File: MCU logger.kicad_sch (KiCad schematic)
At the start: 25 parts, among them U1 24LC1025, U2 24LC1025, U3 DS1337S_, U4 ATMEGA328P-AU, Y1 Crystal, Y2 Crystal

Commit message: value of components
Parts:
- C1, C2: value C -> 0.1 uF
- C3, C4: value C -> 22 pF
- C5: value C_Polarized -> 100 nF
- R1, R2: value R -> 330
- R3, R4: value R -> 10 K
- R5, R6: value R -> 4.7 K
- R7: value R -> 10 k
- Y1: value Crystal -> 16 MHz
- Y2: value Crystal -> 32.768 KHz
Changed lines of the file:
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@@
 			)
 		)
-		(property "Value" "R"
+		(property "Value" "4.7 K"
 			(at 120.65 173.9899 0)
 			(show_name no)
@@
 		)
 		(property "Description" "Resistor"
+			(at 118.11 172.72 0)
+			(hide yes)
+			(show_name no)
+			(do_not_autoplace no)
+			(effects
+				(font
+					(size 1.27 1.27)
+				)
+			)
+		)
+		(property "purpose" ""
 			(at 118.11 172.72 0)
 			(hide yes)
@@
 			)
 		)
-		(property "Value" "R"
+		(property "Value" "330"
 			(at 246.38 71.1199 0)
 			(show_name no)
@@
 		)
 		(property "Description" "Resistor"
+			(at 243.84 69.85 0)
+			(hide yes)
+			(show_name no)
+			(do_not_autoplace no)
+			(effects
+				(font
+					(size 1.27 1.27)
+				)
+			)
+		)
+		(property "purpose" ""
 			(at 243.84 69.85 0)
 			(hide yes)
@@
 			)
 		)
+		(property "purpose" ""
+			(at 262.89 38.1 0)
+			(hide yes)
+			(show_name no)
+			(do_not_autoplace no)
+			(effects
+				(font
+					(size 1.27 1.27)
+				)
+			)
+		)
 		(pin "2"
 		)
@@
 			)
 		)
-		(property "Value" "C"
+		(property "Value" "22 pF"
 			(at 176.53 69.8499 0)
 			(show_name no)
@@
 		)
 		(property "Description" "Unpolarized capacitor"
+			(at 172.72 68.58 0)
+			(hide yes)
+			(show_name no)
+			(do_not_autoplace no)
+			(effects
+				(font
+					(size 1.27 1.27)
+				)
+			)
+		)
+		(property "purpose" ""
 			(at 172.72 68.58 0)
 			(hide yes)
@@
 			)
 		)
-		(property "Value" "R"
+		(property "Value" "10 K"
 			(at 106.68 52.0699 0)
 			(show_name no)
@@
 		)
 		(property "Description" "Resistor"
+			(at 104.14 50.8 0)
+			(hide yes)
+			(show_name no)
+			(do_not_autoplace no)
+			(effects
+				(font
+					(size 1.27 1.27)
+				)
+			)
+		)
+		(property "purpose" ""
 			(at 104.14 50.8 0)
 			(hide yes)
@@
 			)
 		)
-		(property "Value" "R"
+		(property "Value" "330"
 			(at 171.45 39.37 90)
 			(show_name no)
@@
 		)
 		(property "Description" "Resistor"
+			(at 171.45 43.18 0)
+			(hide yes)
+			(show_name no)
+			(do_not_autoplace no)
+			(effects
+				(font
+					(size 1.27 1.27)
+				)
+			)
+		)
+		(property "purpose" ""
 			(at 171.45 43.18 0)
 			(hide yes)
@@
 			)
 		)
-		(property "Value" "R"
+		(property "Value" "4.7 K"
 			(at 109.22 173.9899 0)
 			(show_name no)
@@
 		)
 		(property "Description" "Resistor"
+			(at 106.68 172.72 0)
+			(hide yes)
+			(show_name no)
+			(do_not_autoplace no)
+			(effects
+				(font
+					(size 1.27 1.27)
+				)
+			)
+		)
+		(property "purpose" ""
 			(at 106.68 172.72 0)
 			(hide yes)
@@
 			)
 		)
-		(property "Value" "C_Polarized"
+		(property "Value" "100 nF"
 			(at 247.65 38.4809 0)
 			(show_name no)
@@
 		)
 		(property "Description" "Polarized capacitor"
+			(at 243.84 38.1 0)
+			(hide yes)
+			(show_name no)
+			(do_not_autoplace no)
+			(effects
+				(font
+					(size 1.27 1.27)
+				)
+			)
+		)
+		(property "purpose" ""
 			(at 243.84 38.1 0)
 			(hide yes)
@@
 			)
 		)
-		(property "Value" "Crystal"
+		(property "Value" "32.768 KHz"
 			(at 43.18 50.8 0)
 			(show_name no)
@@
 		)
 		(property "Description" "Two pin crystal"
+			(at 43.18 55.88 0)
+			(hide yes)
+			(show_name no)
+			(do_not_autoplace no)
+			(effects
+				(font
+					(size 1.27 1.27)
+				)
+			)
+		)
+		(property "purpose" ""
 			(at 43.18 55.88 0)
 			(hide yes)
@@
 			)
 		)
-		(property "Value" "C"
+		(property "Value" "0.1 uF"
 			(at 187.96 31.7499 0)
 			(show_name no)
@@
 		)
 		(property "Description" "Unpolarized capacitor"
+			(at 184.15 30.48 0)
+			(hide yes)
+			(show_name no)
+			(do_not_autoplace no)
+			(effects
+				(font
+					(size 1.27 1.27)
+				)
+			)
+		)
+		(property "purpose" ""
 			(at 184.15 30.48 0)
 			(hide yes)
@@
 			)
 		)
-		(property "Value" "R"
+		(property "Value" "10 K"
 			(at 118.11 52.0699 0)
 			(show_name no)
@@
 		)
 		(property "Description" "Resistor"
+			(at 115.57 50.8 0)
+			(hide yes)
+			(show_name no)
+			(do_not_autoplace no)
+			(effects
+				(font
+					(size 1.27 1.27)
+				)
+			)
+		)
+		(property "purpose" ""
 			(at 115.57 50.8 0)
 			(hide yes)
@@
 			)
 		)
-		(property "Value" "R"
+		(property "Value" "10 k"
 			(at 189.23 74.93 90)
 			(show_name no)
@@
 		)
 		(property "Description" "Resistor"
+			(at 189.23 78.74 0)
+			(hide yes)
+			(show_name no)
+			(do_not_autoplace no)
+			(effects
+				(font
+					(size 1.27 1.27)
+				)
+			)
+		)
+		(property "purpose" ""
 			(at 189.23 78.74 0)
 			(hide yes)
@@
 			)
 		)
-		(property "Value" "C"
+		(property "Value" "0.1 uF"
 			(at 128.27 52.0699 0)
 			(show_name no)
@@
 		)
 		(property "Description" "Unpolarized capacitor"
+			(at 124.46 50.8 0)
+			(hide yes)
+			(show_name no)
+			(do_not_autoplace no)
+			(effects
+				(font
+					(size 1.27 1.27)
+				)
+			)
+		)
+		(property "purpose" ""
 			(at 124.46 50.8 0)
 			(hide yes)
@@
 			)
 		)
-		(property "Value" "C"
+		(property "Value" "22 pF"
 			(at 176.53 55.8799 0)
 			(show_name no)
@@
 		)
 		(property "Description" "Unpolarized capacitor"
+			(at 172.72 54.61 0)
+			(hide yes)
+			(show_name no)
+			(do_not_autoplace no)
+			(effects
+				(font
+					(size 1.27 1.27)
+				)
+			)
+		)
+		(property "purpose" ""
 			(at 172.72 54.61 0)
 			(hide yes)
@@
 			)
 		)
-		(property "Value" "Crystal"
+		(property "Value" "16 MHz"
 			(at 184.15 55.88 0)
 			(show_name no)
@@
 			(at 184.15 60.96 0)
 			(hide yes)
+			(show_name no)
+			(do_not_autoplace no)
+			(effects
+				(font
+					(size 1.27 1.27)
+				)
+			)
+		)
+		(property "purpose" ""
+			(at 184.15 60.96 0)
+			(hide yes)

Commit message: footprint assigned
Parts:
- BT1: footprint (none) -> Connector_PinHeader_2.54mm:PinHeader_1x02_P2.54mm_Vertical
- C1, C2, C3, C4, C5: footprint (none) -> Capacitor_SMD:C_0805_2012Metric
- D1, D2: footprint (none) -> LED_SMD:LED_0805_2012Metric
- H1, H2, H3, H4: footprint (none) -> MountingHole:MountingHole_2.1mm
- R1, R2, R3, R4, R5, R6, R7: footprint (none) -> Resistor_SMD:R_0805_2012Metric
- U1, U2: footprint (none) -> Package_SO:SOIC-8_5.3x5.3mm_P1.27mm
- U3: footprint DS1337S_:SOIC127P600X175-8N -> footprints:SOIC127P600X175-8N
- U4: footprint ATMEGA328P-AU:QFP80P900X900X120-32N -> footprints:QFP80P900X900X120-32N
- Y1, Y2: footprint (none) -> Crystal:Crystal_SMD_5032-2Pin_5.0x3.2mm_HandSoldering
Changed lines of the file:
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@@
 			)
 		)
-		(property "Footprint" ""
+		(property "Footprint" "MountingHole:MountingHole_2.1mm"
 			(at 247.65 154.94 0)
 			(hide yes)
@@
 			)
 		)
-		(property "Footprint" ""
+		(property "Footprint" "Resistor_SMD:R_0805_2012Metric"
 			(at 116.332 172.72 90)
 			(hide yes)
@@
 			)
 		)
-		(property "Footprint" ""
+		(property "Footprint" "LED_SMD:LED_0805_2012Metric"
 			(at 243.84 53.34 0)
 			(hide yes)
@@
 			)
 		)
-		(property "Footprint" ""
+		(property "Footprint" "MountingHole:MountingHole_2.1mm"
 			(at 247.65 124.46 0)
 			(hide yes)
@@
 			)
 		)
-		(property "Footprint" ""
+		(property "Footprint" "Resistor_SMD:R_0805_2012Metric"
 			(at 242.062 69.85 90)
 			(hide yes)
@@
 			)
 		)
-		(property "Footprint" ""
+		(property "Footprint" "Connector_PinHeader_2.54mm:PinHeader_1x02_P2.54mm_Vertical"
 			(at 262.89 36.576 90)
 			(hide yes)
@@
 			)
 		)
-		(property "Footprint" ""
+		(property "Footprint" "Capacitor_SMD:C_0805_2012Metric"
 			(at 173.6852 72.39 0)
 			(hide yes)
@@
 			)
 		)
-		(property "Footprint" ""
+		(property "Footprint" "Resistor_SMD:R_0805_2012Metric"
 			(at 102.362 50.8 90)
 			(hide yes)
@@
 			)
 		)
-		(property "Footprint" "DS1337S_:SOIC127P600X175-8N"
+		(property "Footprint" "footprints:SOIC127P600X175-8N"
 			(at 76.2 60.96 0)
 			(hide yes)
@@
 			)
 		)
-		(property "Footprint" ""
+		(property "Footprint" "Resistor_SMD:R_0805_2012Metric"
 			(at 171.45 44.958 90)
 			(hide yes)
@@
 			)
 		)
-		(property "Footprint" ""
+		(property "Footprint" "Resistor_SMD:R_0805_2012Metric"
 			(at 104.902 172.72 90)
 			(hide yes)
@@
 			)
 		)
-		(property "Footprint" ""
+		(property "Footprint" "Package_SO:SOIC-8_5.3x5.3mm_P1.27mm"
 			(at 87.63 173.99 0)
 			(hide yes)
@@
 			)
 		)
-		(property "Footprint" ""
+		(property "Footprint" "Package_SO:SOIC-8_5.3x5.3mm_P1.27mm"
 			(at 53.34 173.99 0)
 			(hide yes)
@@
 			)
 		)
-		(property "Footprint" ""
+		(property "Footprint" "MountingHole:MountingHole_2.1mm"
 			(at 247.65 134.62 0)
 			(hide yes)
@@
 			)
 		)
-		(property "Footprint" "ATMEGA328P-AU:QFP80P900X900X120-32N"
+		(property "Footprint" "footprints:QFP80P900X900X120-32N"
 			(at 214.63 58.42 0)
 			(hide yes)
@@
 			)
 		)
-		(property "Footprint" ""
+		(property "Footprint" "MountingHole:MountingHole_2.1mm"
 			(at 247.65 144.78 0)
 			(hide yes)
@@
 			)
 		)
-		(property "Footprint" ""
+		(property "Footprint" "Capacitor_SMD:C_0805_2012Metric"
 			(at 244.8052 41.91 0)
 			(hide yes)
@@
 			)
 		)
-		(property "Footprint" ""
+		(property "Footprint" "Crystal:Crystal_SMD_5032-2Pin_5.0x3.2mm_HandSoldering"
 			(at 43.18 55.88 0)
 			(hide yes)
@@
 			)
 		)
-		(property "Footprint" ""
+		(property "Footprint" "Capacitor_SMD:C_0805_2012Metric"
 			(at 185.1152 34.29 0)
 			(hide yes)
@@
 			)
 		)
-		(property "Footprint" ""
+		(property "Footprint" "Resistor_SMD:R_0805_2012Metric"
 			(at 113.792 50.8 90)
 			(hide yes)
@@
 			)
 		)
-		(property "Footprint" ""
+		(property "Footprint" "LED_SMD:LED_0805_2012Metric"
 			(at 184.15 43.18 0)
 			(hide yes)
@@
 			)
 		)
-		(property "Footprint" ""
+		(property "Footprint" "Resistor_SMD:R_0805_2012Metric"
 			(at 189.23 80.518 90)
 			(hide yes)
@@
 			)
 		)
-		(property "Footprint" ""
+		(property "Footprint" "Capacitor_SMD:C_0805_2012Metric"
 			(at 125.4252 54.61 0)
 			(hide yes)
@@
 			)
 		)
-		(property "Footprint" ""
+		(property "Footprint" "Capacitor_SMD:C_0805_2012Metric"
 			(at 173.6852 58.42 0)
 			(hide yes)
@@
 			)
 		)
-		(property "Footprint" ""
+		(property "Footprint" "Crystal:Crystal_SMD_5032-2Pin_5.0x3.2mm_HandSoldering"
 			(at 184.15 60.96 0)
 			(hide yes)

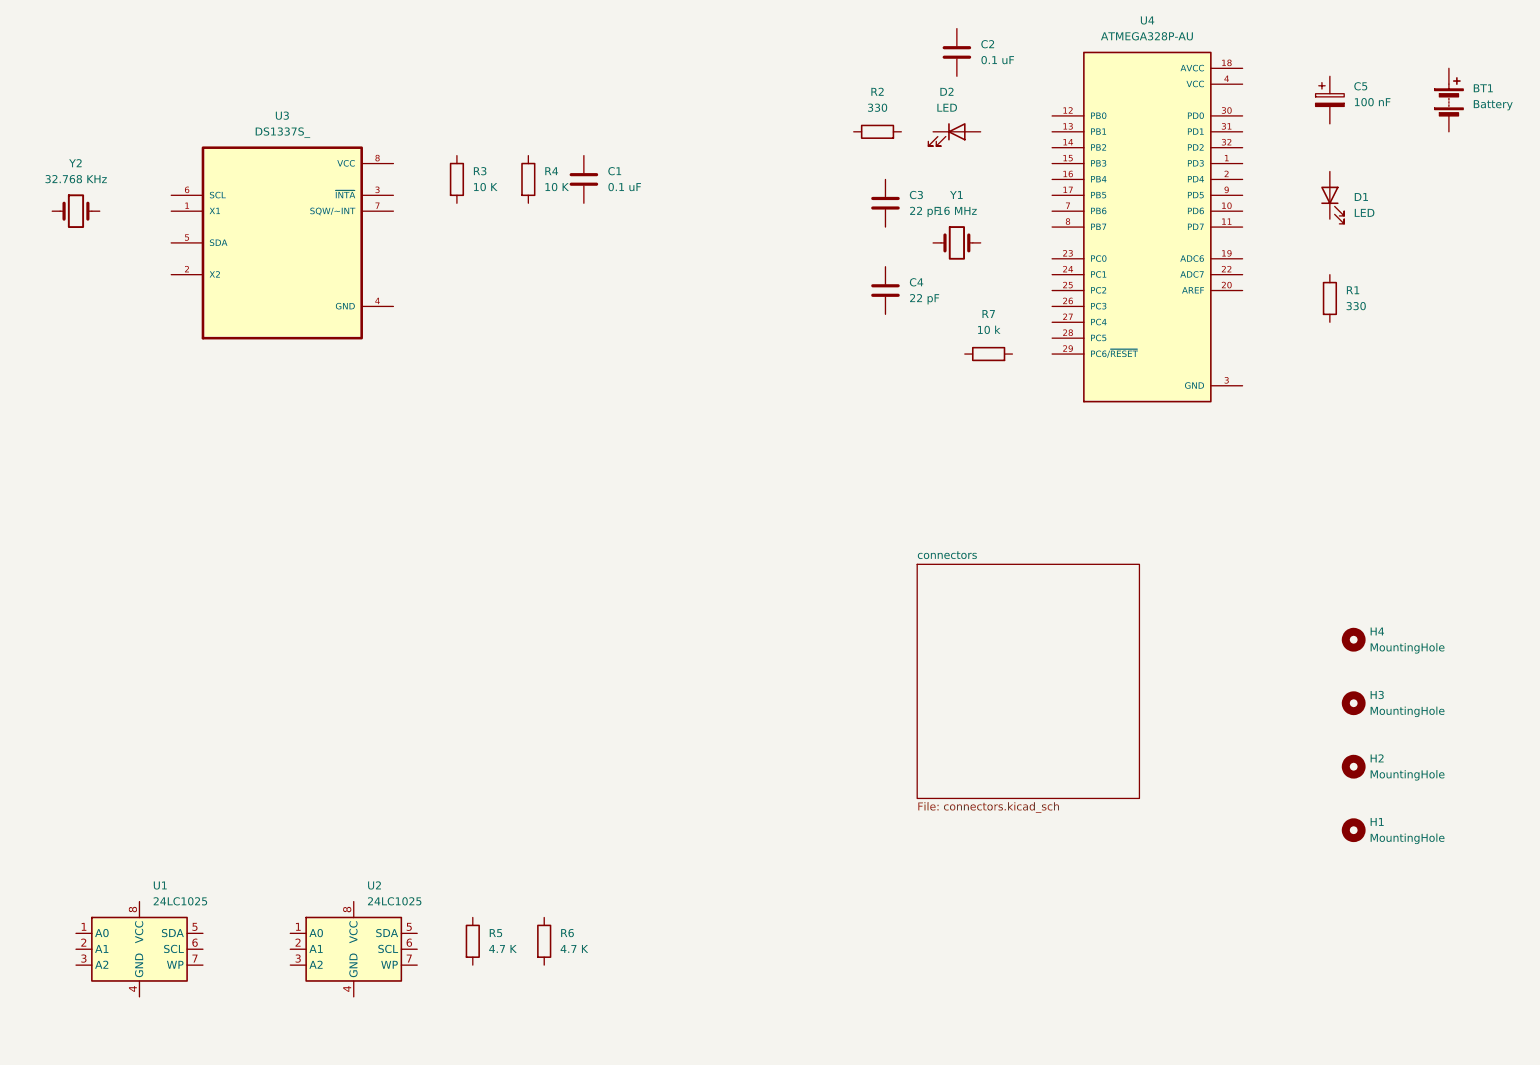
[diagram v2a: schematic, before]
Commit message: wiring of main sheet
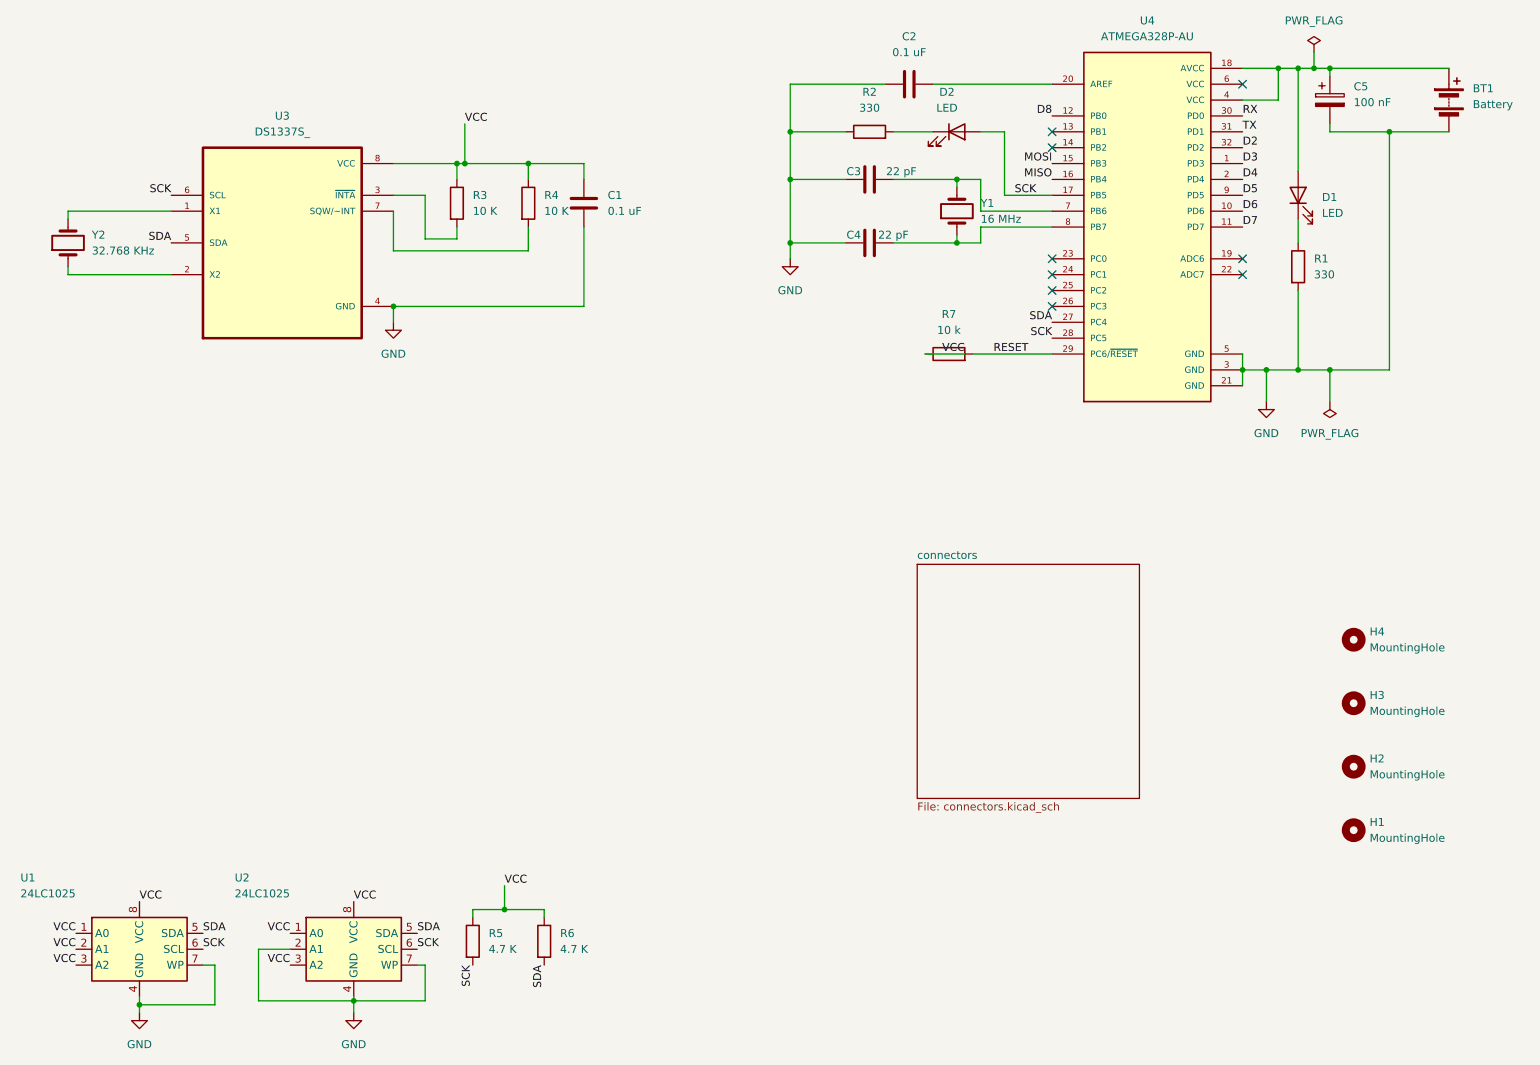
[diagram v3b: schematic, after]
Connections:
- net GND: now also BT1.2 (-), C1.2, C2.1, C3.1, C4.1, C5.2, R1.2, R2.1, U1.4 (GND), U1.7 (WP), U2.2 (A1), U2.4 (GND), U2.7 (WP), U3.4 (GND)
- net VCC: now also C1.1, R3.1, R4.1, R5.1, R6.1, R7.1, U1.1 (A0), U1.2 (A1), U1.3 (A2), U1.8 (VCC), U2.1 (A0), U2.3 (A2), U2.8 (VCC), U3.8 (VCC); no longer U4.4 (VCC), U4.6 (VCC)
- net SDA: now reaches R6.2
- net SDA: now also U1.5 (SDA), U2.5 (SDA), U3.5 (SDA), U4.27 (PC4)
- net at D1.1 (K): now also R1.1
- net at D1.2 (A): now also BT1.1 (+), C5.1, U4.18 (AVCC), U4.4 (VCC)
- net at C4.2: now also U4.8 (PB7), Y1.1
- net at R3.2: now also U3.3 (~{INTA})
- net at U3.1 (X1): now also Y2.2
- net at U3.2 (X2): now also Y2.1
- net SCK: now reaches U3.6 (SCL)
- net SCK: now also D2.2 (A), R5.2, U1.6 (SCL), U2.6 (SCL), U4.17 (PB5), U4.28 (PC5)
- net at U3.7 (SQW/~INT): now also R4.2
- net at R2.2: now also D2.1 (K)
- net D3: now reaches U4.1 (PD3)
- net D6: now reaches U4.10 (PD6)
- net D7: now reaches U4.11 (PD7)
- net D8: now reaches U4.12 (PB0)
- net MOSI: now reaches U4.15 (PB3)
- net MISO: now reaches U4.16 (PB4)
- net D4: now reaches U4.2 (PD4)
- net at U4.20 (AREF): now also C2.2
- net RESET: now reaches U4.29 (PC6/~{RESET})
- net RESET: now also R7.2
- net RX: now reaches U4.30 (PD0)
- net TX: now reaches U4.31 (PD1)
- net D2: now reaches U4.32 (PD2)
- net at U4.7 (PB6): now also C3.2, Y1.2
- net D5: now reaches U4.9 (PD5)
- no-connect marks 0 -> 9
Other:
- moved on the sheet: C1, C2, C3, C4, D1, R1, R2, R3, R4, R7, Y1, Y2

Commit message: wiring complete
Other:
- sheet connectors ports: added D2, D3, D4, D5, D6, D7, D8, GND, MISO, MOSI, RESET, RX, SCK, SDA, TX, VCC; removed none
- moved on the sheet: R5, R6, U1, U2
